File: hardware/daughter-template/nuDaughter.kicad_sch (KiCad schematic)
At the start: 1 part, among them J1 nuMezzanine_4x34

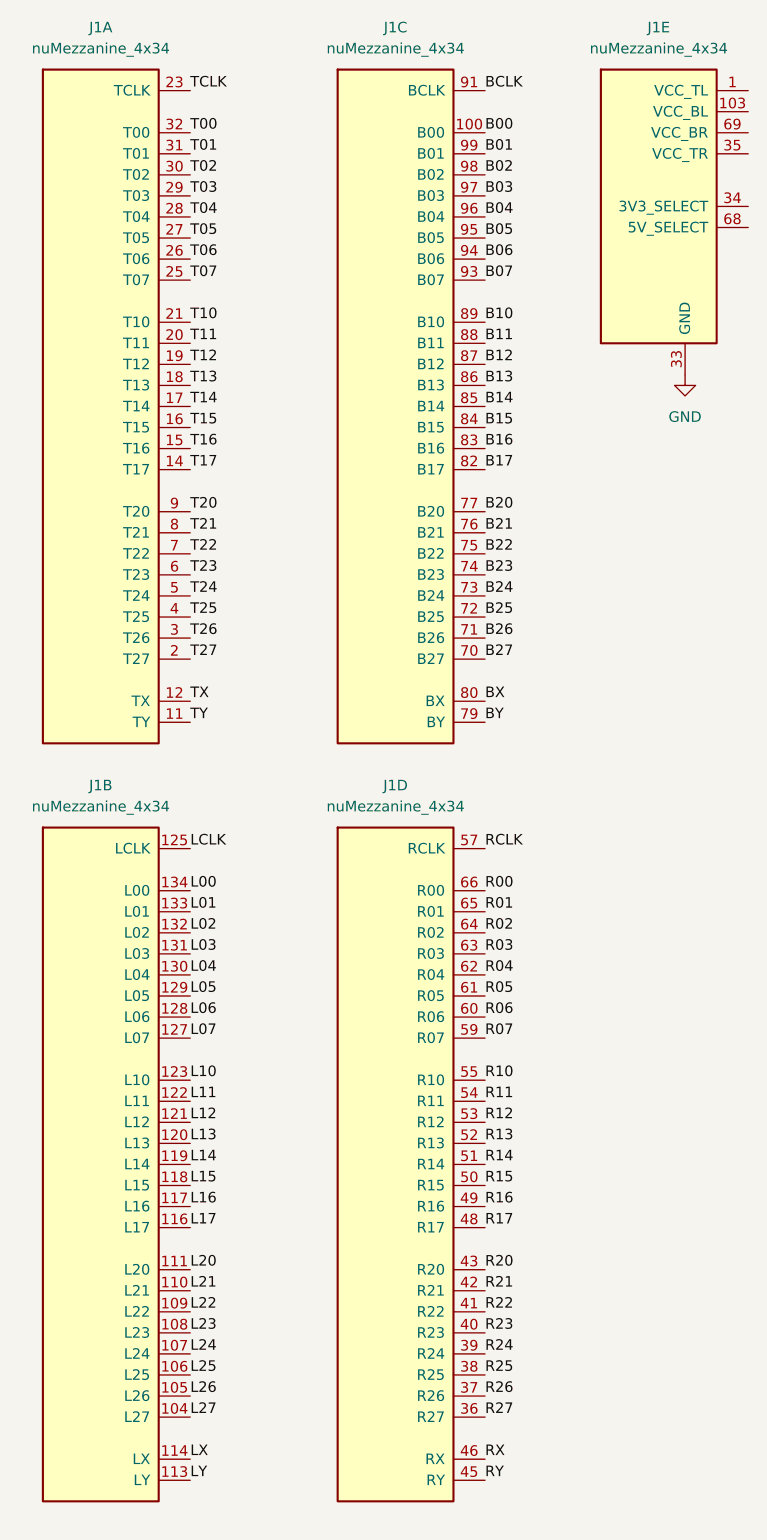
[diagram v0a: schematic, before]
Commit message: Update mainboard to revision 2
Add an additional 8 bidirectional channels
Replace SPI PSRAM with hyperram
Remove LEDs
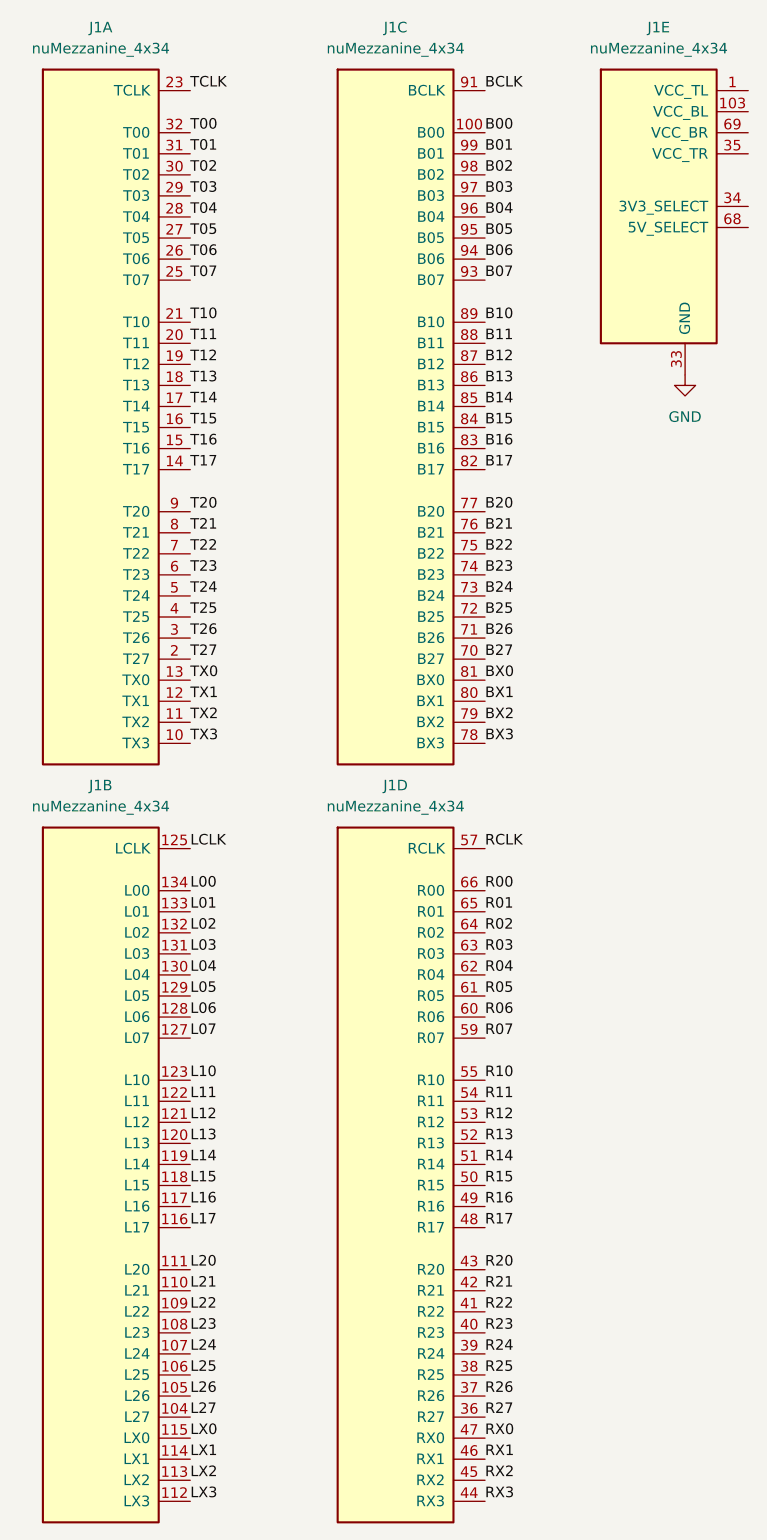
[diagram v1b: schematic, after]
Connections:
- net GND: now also J1.102 (GND), J1.136 (GND); no longer J1.10 (GND), J1.112 (GND), J1.115 (GND), J1.13 (GND), J1.44 (GND), J1.47 (GND), J1.78 (GND), J1.81 (GND)
- net BX renamed BX1
- net BY renamed BX2
- net LX renamed LX1
- net LY renamed LX2
- net RX renamed RX1
- net RY renamed RX2
- net TX renamed TX1
- net TY renamed TX2
- new net BX0: J1.81 (BX0)
- new net BX3: J1.78 (BX3)
- new net LX0: J1.115 (LX0)
- new net LX3: J1.112 (LX3)
- new net RX0: J1.47 (RX0)
- new net RX3: J1.44 (RX3)
- new net TX0: J1.13 (TX0)
- new net TX3: J1.10 (TX3)
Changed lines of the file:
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@@
 		)
 	)
-	(label "TX"
+	(label "TX1"
 		(at 36.83 97.79 0)
 		(effects
@@
 		)
 	)
-	(label "LY"
+	(label "LX2"
 		(at 36.83 191.77 0)
 		(effects
@@
 		)
 	)
-	(label "BY"
+	(label "BX2"
 		(at 72.39 100.33 0)
 		(effects
@@
 		)
 	)
-	(label "RX"
+	(label "RX1"
 		(at 72.39 189.23 0)
 		(effects
@@
 		)
 	)
-	(label "BX"
+	(label "BX1"
 		(at 72.39 97.79 0)
 		(effects
@@
 		)
 	)
-	(label "TY"
+	(label "TX2"
 		(at 36.83 100.33 0)
 		(effects
@@
 		)
 	)
-	(label "RY"
+	(label "RX2"
 		(at 72.39 191.77 0)
 		(effects
@@
 		)
 	)
-	(label "LX"
+	(label "LX1"
 		(at 36.83 189.23 0)
 		(effects
@@
 	)
 	(embedded_fonts no)
+(label "LX0" (at 36.83 186.69 0) (effects (font (size 1.27 1.27)) (justify left bottom)))
+(label "LX3" (at 36.83 194.31 0) (effects (font (size 1.27 1.27)) (justify left bottom)))
+(label "TX0" (at 36.83 95.25 0) (effects (font (size 1.27 1.27)) (justify left bottom)))
+(label "TX3" (at 36.83 102.87 0) (effects (font (size 1.27 1.27)) (justify left bottom)))
+(label "RX0" (at 72.39 186.69 0) (effects (font (size 1.27 1.27)) (justify left bottom)))
+(label "RX3" (at 72.39 194.31 0) (effects (font (size 1.27 1.27)) (justify left bottom)))
+(label "BX0" (at 72.39 95.25 0) (effects (font (size 1.27 1.27)) (justify left bottom)))
+(label "BX3" (at 72.39 102.87 0) (effects (font (size 1.27 1.27)) (justify left bottom)))
 )
